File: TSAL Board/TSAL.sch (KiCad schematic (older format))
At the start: 27 parts, among them P1 TS_VCC, P2 TSAL, P4 ACC_LED, Q1 BSS84, Q2 BSS138, SW1 SW_PUSH, SW2 SW_PUSH, U2 TL431, U6 BTS6133D

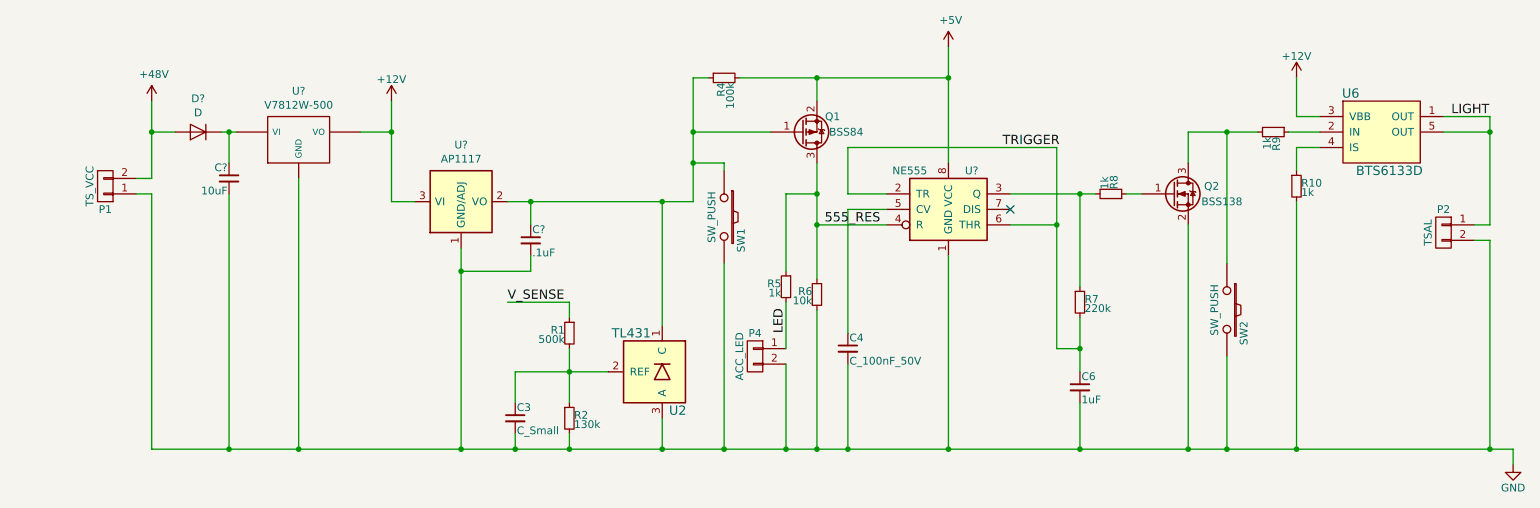
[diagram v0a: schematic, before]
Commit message: Small TSAL changes
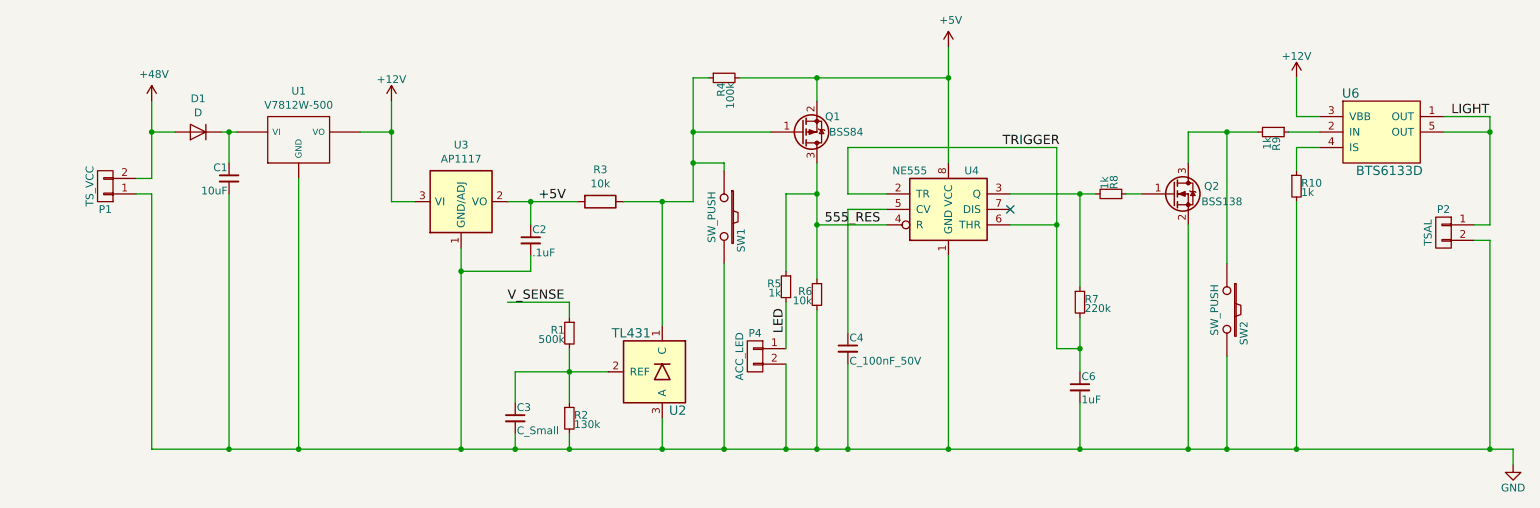
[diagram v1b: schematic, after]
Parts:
- added R3: 10k, symbol R
- gave numbers to parts that had none: 6
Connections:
- net +5V: now also C2.1, U3.2 (VO), U3.4 (VO), R3.2
- net at Q1.1 (G), R4.1, SW1.1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: now also R3.1; no longer C2.1, U3.2 (VO), U3.4 (VO)
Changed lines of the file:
@@
 $EndComp
 $Comp
-L +12V #PWR15
+L +12V #PWR01
 U 1 1 5765272C
 P 8800 2550
-F 0 "#PWR15" H 8800 2400 50  0001 C CNN
+F 0 "#PWR01" H 8800 2400 50  0001 C CNN
 F 1 "+12V" H 8800 2690 50  0000 C CNN
 F 2 "" H 8800 2550 50  0000 C CNN
@@
 $EndComp
 $Comp
-L GND #PWR16
+L GND #PWR02
 U 1 1 5765F5DB
 P 10200 5050
-F 0 "#PWR16" H 10200 4800 50  0001 C CNN
+F 0 "#PWR02" H 10200 4800 50  0001 C CNN
 F 1 "GND" H 10200 4900 50  0000 C CNN
 F 2 "" H 10200 5050 50  0000 C CNN
@@
 $EndComp
 $Comp
-L NE555 U?
+L NE555 U4
 U 1 1 586858A5
 P 6550 3400
-F 0 "U?" H 6700 3650 50  0000 C CNN
+F 0 "U4" H 6700 3650 50  0000 C CNN
 F 1 "NE555" H 6300 3650 50  0000 C CNN
 F 2 "" H 6550 3400 50  0000 C CNN
@@
 V_SENSE
 $Comp
-L V7812W-500 U?
+L V7812W-500 U1
 U 1 1 58688F32
 P 2350 2950
-F 0 "U?" H 2350 3265 50  0000 C CNN
+F 0 "U1" H 2350 3265 50  0000 C CNN
 F 1 "V7812W-500" H 2350 3174 50  0000 C CNN
 F 2 "" H 2350 2950 50  0000 C CNN
@@
 $EndComp
 $Comp
-L AP1117 U?
+L AP1117 U3
 U 1 1 58689294
 P 3400 3350
-F 0 "U?" H 3400 3717 50  0000 C CNN
+F 0 "U3" H 3400 3717 50  0000 C CNN
 F 1 "AP1117" H 3400 3626 50  0000 C CNN
 F 2 "TO_SOT_Packages_SMD:SOT-223" H 3400 3000 50  0001 C CNN
@@
 $EndComp
 $Comp
-L C_Small C?
+L C_Small C2
 U 1 1 5868A562
 P 3850 3600
-F 0 "C?" H 3860 3670 50  0000 L CNN
+F 0 "C2" H 3860 3670 50  0000 L CNN
 F 1 ".1uF" H 3860 3520 50  0000 L CNN
 F 2 "Tinkercad:0805" H 3850 3600 50  0001 C CNN
@@
 $EndComp
 $Comp
-L +12V #PWR?
+L +12V #PWR03
 U 1 1 5868B7CE
 P 2950 2700
-F 0 "#PWR?" H 2950 2550 50  0001 C CNN
+F 0 "#PWR03" H 2950 2550 50  0001 C CNN
 F 1 "+12V" H 2950 2840 50  0000 C CNN
 F 2 "" H 2950 2700 50  0000 C CNN
@@
 $EndComp
 $Comp
-L +48V #PWR?
+L +48V #PWR04
 U 1 1 5868F5B1
 P 1400 2700
-F 0 "#PWR?" H 1400 2550 50  0001 C CNN
+F 0 "#PWR04" H 1400 2550 50  0001 C CNN
 F 1 "+48V" H 1415 2873 50  0000 C CNN
 F 2 "" H 1400 2700 50  0000 C CNN
@@
 $EndComp
 $Comp
-L D D?
+L D D1
 U 1 1 5869031C
 P 1700 2900
-F 0 "D?" H 1700 2684 50  0000 C CNN
+F 0 "D1" H 1700 2684 50  0000 C CNN
 F 1 "D" H 1700 2775 50  0000 C CNN
 F 2 "" H 1700 2900 50  0000 C CNN
@@
 $EndComp
 $Comp
-L C_Small C?
+L C_Small C1
 U 1 1 586905E1
 P 1900 3200
-F 0 "C?" H 1910 3270 50  0000 L CNN
+F 0 "C1" H 1910 3270 50  0000 L CNN
 F 1 "10uF" H 1910 3120 50  0000 L CNN
 F 2 "Tinkercad:0805" H 1900 3200 50  0001 C CNN
@@
 $EndComp
 Wire Wire Line
-	3750 4450 4100 4450
-Wire Wire Line
-	4100 4450 4350 4450
-Wire Wire Line
-	4100 4300 4100 4450
-Wire Wire Line
-	4100 4450 4100 4650
+	3750 4450 4350 4450
+Wire Wire Line
+	4100 4300 4100 4650
 Connection ~ 4100 4450
 Wire Wire Line
@@
 	4100 4000 4100 4100
 Wire Wire Line
-	10050 2800 10050 2900
-Wire Wire Line
-	10050 2900 10050 3500
+	10050 2800 10050 3500
 Wire Wire Line
 	10050 3500 9950 3500
@@
 	8950 2900 8750 2900
 Wire Wire Line
-	4900 3350 4900 3100
-Wire Wire Line
-	4900 3100 4900 2900
-Wire Wire Line
-	4900 2900 4900 2550
-Wire Wire Line
-	3700 3350 3850 3350
-Wire Wire Line
-	3850 3350 4700 3350
-Wire Wire Line
-	4700 3350 4900 3350
+	4900 3350 4900 2550
+Wire Wire Line
+	3700 3350 4150 3350
+Wire Wire Line
+	4450 3350 4900 3350
 Wire Wire Line
 	5400 2900 4900 2900
 Wire Wire Line
-	5200 2550 5700 2550
-Wire Wire Line
-	5700 2550 6550 2550
+	5200 2550 6550 2550
 Wire Wire Line
 	5700 2550 5700 2700
@@
 	5700 3500 6150 3500
 Wire Wire Line
-	5700 3100 5700 3300
-Wire Wire Line
-	5700 3300 5700 3500
-Wire Wire Line
-	5700 3500 5700 3850
-Wire Wire Line
-	1400 4950 1900 4950
-Wire Wire Line
-	1900 4950 2350 4950
-Wire Wire Line
-	2350 4950 3400 4950
-Wire Wire Line
-	3400 4950 3750 4950
-Wire Wire Line
-	3750 4950 4100 4950
-Wire Wire Line
-	4100 4950 4700 4950
-Wire Wire Line
-	4700 4950 5100 4950
-Wire Wire Line
-	5100 4950 5500 4950
-Wire Wire Line
-	5500 4950 5700 4950
-Wire Wire Line
-	5700 4950 5900 4950
-Wire Wire Line
-	5900 4950 6550 4950
-Wire Wire Line
-	6550 4950 7400 4950
-Wire Wire Line
-	7400 4950 8100 4950
-Wire Wire Line
-	8100 4950 8350 4950
-Wire Wire Line
-	8350 4950 8800 4950
-Wire Wire Line
-	8800 4950 10050 4950
-Wire Wire Line
-	10050 4950 10200 4950
+	5700 3100 5700 3850
+Wire Wire Line
+	1400 4950 10200 4950
 Connection ~ 5700 2550
 Connection ~ 5700 3500
@@
 Connection ~ 6550 4950
 Wire Wire Line
-	6550 2350 6550 2550
-Wire Wire Line
-	6550 2550 6550 3100
+	6550 2350 6550 3100
 Connection ~ 6550 2550
 Wire Wire Line
@@
 	5900 3000 7250 3000
 Wire Wire Line
-	7250 3000 7250 3500
-Wire Wire Line
-	7250 3500 7250 4300
+	7250 3000 7250 4300
 Wire Wire Line
 	6950 3500 7250 3500
 Wire Wire Line
-	7400 4100 7400 4300
-Wire Wire Line
-	7400 4300 7400 4450
+	7400 4100 7400 4450
 Wire Wire Line
 	7400 4650 7400 4950
@@
 Connection ~ 5900 4950
 Wire Wire Line
-	6950 3300 7400 3300
-Wire Wire Line
-	7400 3300 7500 3300
+	6950 3300 7500 3300
 Wire Wire Line
 	7400 3300 7400 3900
 Connection ~ 7400 3300
 Wire Wire Line
-	8100 2900 8350 2900
-Wire Wire Line
-	8350 2900 8550 2900
+	8100 2900 8550 2900
 Wire Wire Line
 	8100 2900 8100 3100
@@
 Connection ~ 4700 3350
 Wire Wire Line
-	3400 3650 3400 3800
-Wire Wire Line
-	3400 3800 3400 4950
+	3400 3650 3400 4950
 Connection ~ 3750 4950
 Wire Wire Line
@@
 Connection ~ 3400 3800
 Wire Wire Line
-	3850 3500 3850 3350
+	3850 3350 3850 3500
 Connection ~ 3850 3350
 Wire Wire Line
@@
 	1400 3200 1300 3200
 Wire Wire Line
-	1400 2700 1400 2900
-Wire Wire Line
-	1400 2900 1400 3200
+	1400 2700 1400 3200
 Connection ~ 1400 2900
 Wire Wire Line
 	1400 2900 1550 2900
 Wire Wire Line
-	1850 2900 1900 2900
-Wire Wire Line
-	1900 2900 1950 2900
+	1850 2900 1950 2900
 Wire Wire Line
 	1900 3100 1900 2900
@@
 Connection ~ 2350 4950
 Wire Wire Line
-	2950 2700 2950 2900
-Wire Wire Line
-	2950 2900 2950 3350
-$Comp
-L +5V #PWR?
+	2950 2700 2950 3350
+$Comp
+L +5V #PWR05
 U 1 1 58693C0C
 P 6550 2350
-F 0 "#PWR?" H 6550 2200 50  0001 C CNN
+F 0 "#PWR05" H 6550 2200 50  0001 C CNN
 F 1 "+5V" H 6565 2523 50  0000 C CNN
 F 2 "" H 6550 2350 50  0000 C CNN
@@
 	1400 3300 1400 4950
 Connection ~ 1900 4950
+$Comp
+L R R3
+U 1 1 586B0DF5
+P 4300 3350
+F 0 "R3" V 4093 3350 50  0000 C CNN
+F 1 "10k" V 4184 3350 50  0000 C CNN
+F 2 "" V 4230 3350 50  0000 C CNN
+F 3 "" H 4300 3350 50  0000 C CNN
+	1    4300 3350
+	0    1    1    0
+$EndComp
+Text Label 3900 3350 0    60   ~ 0
++5V
 $EndSCHEMATC

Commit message: ESF updates, TSAL board updates
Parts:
- removed R9: 1k, Tinkercad:0805, symbol R_Small
- removed SW1, SW2: SW_PUSH, Wetmelon:B3U-1100P, symbol SW_PUSH
- added F?: Polyfuse, symbol Polyfuse
- added SW? (x2): SW_Push, symbol SW_Push
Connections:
- net +48V: now also F?.2; no longer D1.2 (A)
- net GND: now also SW?.2, SW?.2
- net at Q1.1 (G), R3.1, R4.1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: now also SW?.1
- net at U6.2 (IN): now also Q2.3 (D), SW?.1
- new net: D1.2 (A), F?.1
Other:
- moved on the sheet: P1
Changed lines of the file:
@@
 LIBS:contrib
 LIBS:valves
+LIBS:switches
 LIBS:TSAL-cache
 EELAYER 26 0
@@
 $EndComp
 $Comp
-L R_Small R9
-U 1 1 57664DD7
-P 8650 2900
-F 0 "R9" H 8680 2920 50  0000 L CNN
-F 1 "1k" H 8680 2860 50  0000 L CNN
-F 2 "Tinkercad:0805" H 8650 2900 50  0001 C CNN
-F 3 "" H 8650 2900 50  0000 C CNN
-	1    8650 2900
-	0    1    1    0
-$EndComp
-$Comp
-L SW_PUSH SW2
-U 1 1 5765B923
-P 8350 4050
-F 0 "SW2" H 8500 4160 50  0000 C CNN
-F 1 "SW_PUSH" H 8350 3970 50  0000 C CNN
-F 2 "Wetmelon:B3U-1100P" H 8350 4050 50  0001 C CNN
-F 3 "" H 8350 4050 50  0000 C CNN
-	1    8350 4050
-	0    1    1    0
-$EndComp
-$Comp
-L SW_PUSH SW1
-U 1 1 5765BED8
-P 5100 3450
-F 0 "SW1" H 5250 3560 50  0000 C CNN
-F 1 "SW_PUSH" H 5100 3370 50  0000 C CNN
-F 2 "Wetmelon:B3U-1100P" H 5100 3450 50  0001 C CNN
-F 3 "" H 5100 3450 50  0000 C CNN
-	1    5100 3450
-	0    1    1    0
-$EndComp
-$Comp
 L CONN_01X02 P4
 U 1 1 5766F536
@@
 L CONN_01X02 P1
 U 1 1 575A1492
-P 1100 3250
-F 0 "P1" H 1100 3400 50  0000 C CNN
-F 1 "TS_VCC" V 1200 3250 50  0000 C CNN
-F 2 "Terminal_Blocks:TerminalBlock_Pheonix_PT-3.5mm_2pol" H 1100 3250 50  0001 C CNN
-F 3 "" H 1100 3250 50  0000 C CNN
-	1    1100 3250
+P 650 3250
+F 0 "P1" H 650 3400 50  0000 C CNN
+F 1 "TS_VCC" V 750 3250 50  0000 C CNN
+F 2 "Terminal_Blocks:TerminalBlock_Pheonix_PT-3.5mm_2pol" H 650 3250 50  0001 C CNN
+F 3 "" H 650 3250 50  0000 C CNN
+	1    650  3250
 	-1   0    0    1
 $EndComp
@@
 L +48V #PWR04
 U 1 1 5868F5B1
-P 1400 2700
-F 0 "#PWR04" H 1400 2550 50  0001 C CNN
-F 1 "+48V" H 1415 2873 50  0000 C CNN
-F 2 "" H 1400 2700 50  0000 C CNN
-F 3 "" H 1400 2700 50  0000 C CNN
-	1    1400 2700
+P 950 2700
+F 0 "#PWR04" H 950 2550 50  0001 C CNN
+F 1 "+48V" H 965 2873 50  0000 C CNN
+F 2 "" H 950 2700 50  0000 C CNN
+F 3 "" H 950 2700 50  0000 C CNN
+	1    950  2700
 	1    0    0    -1
 $EndComp
@@
 Connection ~ 10050 2900
 Wire Wire Line
-	8950 2900 8750 2900
+	8100 2900 8950 2900
 Wire Wire Line
 	4900 3350 4900 2550
@@
 	5700 3100 5700 3850
 Wire Wire Line
-	1400 4950 10200 4950
+	950  4950 10200 4950
 Connection ~ 5700 2550
 Connection ~ 5700 3500
@@
 Connection ~ 7400 3300
 Wire Wire Line
-	8100 2900 8550 2900
-Wire Wire Line
 	8100 2900 8100 3100
 Wire Wire Line
@@
 	9950 3600 10050 3600
 Wire Wire Line
-	8350 3750 8350 2900
+	8350 2900 8350 3850
 Connection ~ 8350 2900
 Wire Wire Line
-	8350 4350 8350 4950
+	8350 4250 8350 4950
 Connection ~ 8350 4950
 Wire Wire Line
-	5100 3750 5100 4950
+	5100 3550 5100 4950
 Connection ~ 5100 4950
 Wire Wire Line
@@
 Connection ~ 10050 4950
 Wire Wire Line
-	1400 3200 1300 3200
-Wire Wire Line
-	1400 2700 1400 3200
-Connection ~ 1400 2900
-Wire Wire Line
-	1400 2900 1550 2900
+	950  3200 850  3200
+Wire Wire Line
+	950  2700 950  3200
+Connection ~ 950  2900
 Wire Wire Line
 	1850 2900 1950 2900
@@
 $EndComp
 Wire Wire Line
-	1300 3300 1400 3300
-Wire Wire Line
-	1400 3300 1400 4950
+	850  3300 950  3300
+Wire Wire Line
+	950  3300 950  4950
 Connection ~ 1900 4950
 $Comp
@@
 Text Label 3900 3350 0    60   ~ 0
 +5V
+$Comp
+L SW_Push SW?
+U 1 1 5875913B
+P 8350 4050
+F 0 "SW?" V 8304 4198 50  0000 L CNN
+F 1 "SW_Push" V 8395 4198 50  0000 L CNN
+F 2 "" H 8350 4250 50  0000 C CNN
+F 3 "" H 8350 4250 50  0000 C CNN
+	1    8350 4050
+	0    1    1    0
+$EndComp
+$Comp
+L SW_Push SW?
+U 1 1 587594BA
+P 5100 3350
+F 0 "SW?" V 5054 3498 50  0000 L CNN
+F 1 "SW_Push" V 5145 3498 50  0000 L CNN
+F 2 "" H 5100 3550 50  0000 C CNN
+F 3 "" H 5100 3550 50  0000 C CNN
+	1    5100 3350
+	0    1    1    0
+$EndComp
+$Comp
+L Polyfuse F?
+U 1 1 5875A3A3
+P 1250 2900
+F 0 "F?" V 1025 2900 50  0000 C CNN
+F 1 "Polyfuse" V 1116 2900 50  0000 C CNN
+F 2 "" H 1300 2700 50  0001 L CNN
+F 3 "" H 1250 2900 50  0001 C CNN
+	1    1250 2900
+	0    1    1    0
+$EndComp
+Wire Wire Line
+	1100 2900 950  2900
+Wire Wire Line
+	1400 2900 1550 2900
 $EndSCHEMATC
